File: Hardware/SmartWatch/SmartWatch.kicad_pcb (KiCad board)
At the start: 2 copper layers, 31 parts, among them IC1 DA14683-00000U22, IC2 SPG08P4HM4H-1, IC3 MC3630, J1 Charging Port, M1 c0720b001f, Q1 ECH8693R-TL-W, Q2 ECH8693R-TL-W, U1 BQ297xy, U2 ATmega328P-MMH, U3 W25Q128JVS, U4 MAX30100EFD+, Y1 16Mhz

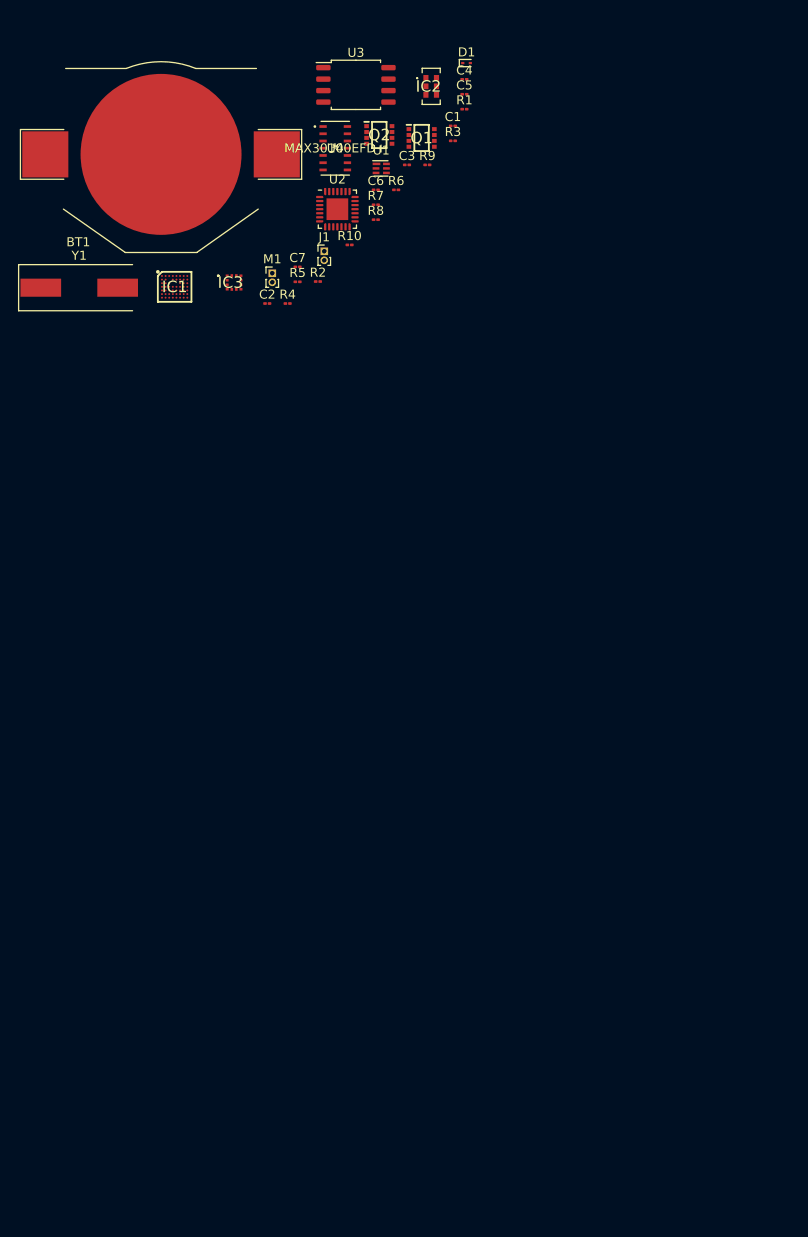
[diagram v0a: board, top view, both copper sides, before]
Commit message: [Update] Wired Display connector to MCU.
Communication type: SPI
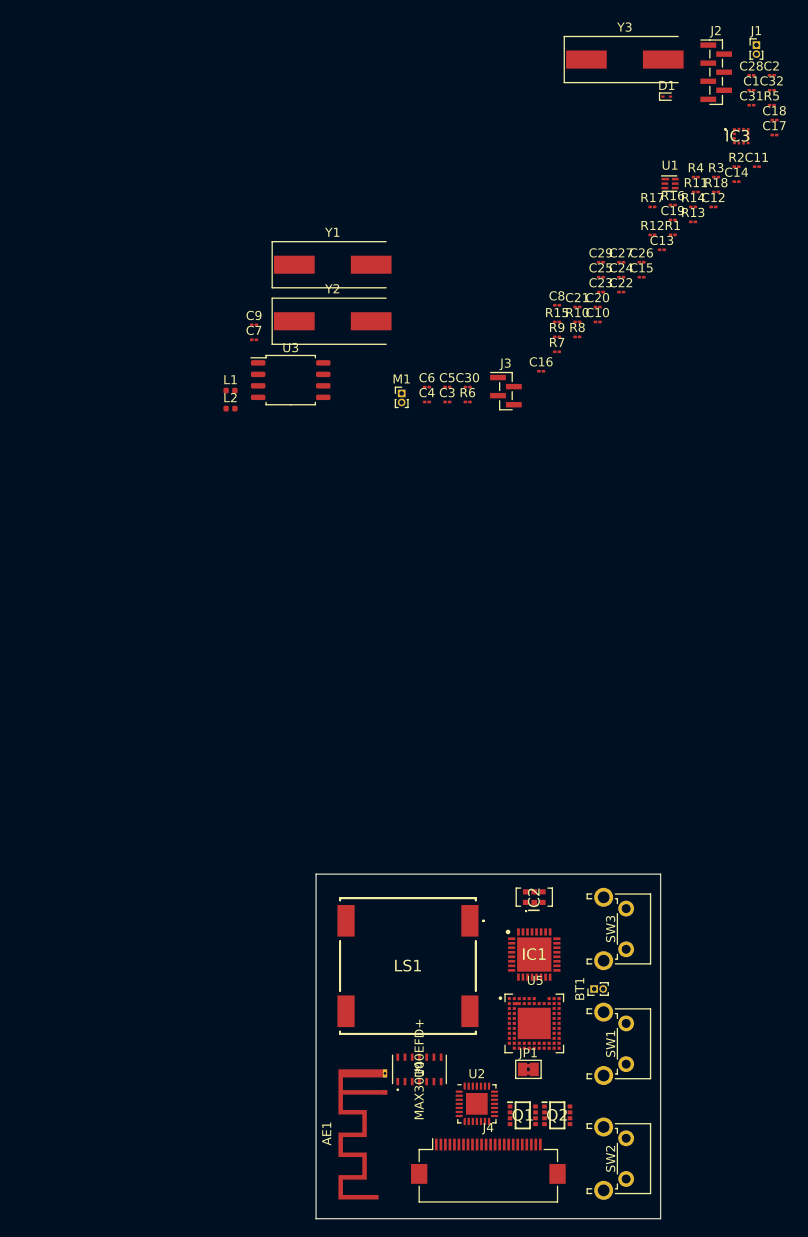
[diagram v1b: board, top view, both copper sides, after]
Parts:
- added AE1: Antenna, RF_Antenna:Texas_SWRA117D_2.4GHz_Left, F.Cu at (109.2, 74.9)
- added C10: 1uF, Capacitor_SMD:C_01005_0402Metric, F.Cu at (132.7, -10.3)
- added C11: 1uF, Capacitor_SMD:C_01005_0402Metric, F.Cu at (150.3, -27.4)
- added C12: 4.7uF, Capacitor_SMD:C_01005_0402Metric, F.Cu at (145.5, -23.0)
- added C13: 4.7uF, Capacitor_SMD:C_01005_0402Metric, F.Cu at (139.8, -18.2)
- added C14: 10uF, Capacitor_SMD:C_01005_0402Metric, F.Cu at (148.1, -25.8)
- added C15: 10uF, Capacitor_SMD:C_01005_0402Metric, F.Cu at (137.6, -15.2)
- added C16: 4.7uF, Capacitor_SMD:C_01005_0402Metric, F.Cu at (126.5, -4.81)
- added C17: 10uF, Capacitor_SMD:C_01005_0402Metric, F.Cu at (152.3, -30.9)
- added C18: 100nF, Capacitor_SMD:C_01005_0402Metric, F.Cu at (152.3, -32.6)
- added C19: 10nF, Capacitor_SMD:C_01005_0402Metric, F.Cu at (141.0, -21.5)
- added C20: 10nF, Capacitor_SMD:C_01005_0402Metric, F.Cu at (132.7, -11.9)
- added C21: C, Capacitor_SMD:C_01005_0402Metric, F.Cu at (130.5, -11.9)
- added C22: C, Capacitor_SMD:C_01005_0402Metric, F.Cu at (135.3, -13.6)
- added C23: 10uF, Capacitor_SMD:C_01005_0402Metric, F.Cu at (133.1, -13.6)
- added C24: 0.1uF, Capacitor_SMD:C_01005_0402Metric, F.Cu at (135.3, -15.2)
- added C25: 10uF, Capacitor_SMD:C_01005_0402Metric, F.Cu at (133.1, -15.2)
- added C26: 0.1uF, Capacitor_SMD:C_01005_0402Metric, F.Cu at (137.6, -16.9)
- added C27: 0.1uF, Capacitor_SMD:C_01005_0402Metric, F.Cu at (135.3, -16.9)
- added C28: 10uF, Capacitor_SMD:C_01005_0402Metric, F.Cu at (149.7, -37.5)
- added C29: 10uF, Capacitor_SMD:C_01005_0402Metric, F.Cu at (133.1, -16.9)
- added C30: 10uF, Capacitor_SMD:C_01005_0402Metric, F.Cu at (118.4, -3.06)
- added C31: 0.1uF, Capacitor_SMD:C_01005_0402Metric, F.Cu at (149.7, -34.2)
- added C32: 0.1uF, Capacitor_SMD:C_01005_0402Metric, F.Cu at (152.0, -35.9)
- added C8: 4.7uF, Capacitor_SMD:C_01005_0402Metric, F.Cu at (128.2, -12.1)
- added C9: 1uF, Capacitor_SMD:C_01005_0402Metric, F.Cu at (94.7, -9.94)
- added J2: DA_PROG_CONN, Connector_PinHeader_1.00mm:PinHeader_1x07_P1.00mm_Vertical_SMD_Pin1Left, F.Cu at (145.8, -37.9)
- added J3: ARD_PROG_CONN, Connector_PinHeader_1.00mm:PinHeader_1x04_P1.00mm_Vertical_SMD_Pin1Left, F.Cu at (122.6, -2.61)
- added J4: Adafruit 4520, Connector_FFC-FPC:Hirose_FH12-24S-0.5SH_1x24-1MP_P0.50mm_Horizontal, F.Cu at (120.7, 82.5)
- added JP1: Jumper, Jumper:SolderJumper-2_P1.3mm_Bridged2Bar_Pad1.0x1.5mm, F.Cu at (125.1, 72.4)
- added L1: 470nH, Inductor_SMD:L_0402_1005Metric, F.Cu at (92.1, -2.67)
- added L2: 470nH, Inductor_SMD:L_0402_1005Metric, F.Cu at (92.1, -0.68)
- added LS1: SMS-1508MS-HT-R, SamacSys_Parts:SMS1508MSHTR, F.Cu at (111.8, 61.0)
- added R11: 100m, Resistor_SMD:R_01005_0402Metric, F.Cu at (143.6, -24.6)
- added R12: 10K, Resistor_SMD:R_01005_0402Metric, F.Cu at (138.8, -19.9)
- added R13: 10K, Resistor_SMD:R_01005_0402Metric, F.Cu at (143.3, -21.3)
- added R14: 10K, Resistor_SMD:R_01005_0402Metric, F.Cu at (143.3, -23.0)
- added R15: 10K, Resistor_SMD:R_01005_0402Metric, F.Cu at (128.2, -10.3)
- added R16: 3.3K, Resistor_SMD:R_01005_0402Metric, F.Cu at (141.0, -23.2)
- added R17: 3.3K, Resistor_SMD:R_01005_0402Metric, F.Cu at (138.8, -23.0)
- added R18: 3.3K, Resistor_SMD:R_01005_0402Metric, F.Cu at (145.8, -24.6)
- added SW1: SW_MEC_5E, Button_Switch_THT:SW_Tactile_SPST_Angled_PTS645Vx58-2LFS, F.Cu at (135.9, 67.3)
- added SW2: SW_MEC_5E, Button_Switch_THT:SW_Tactile_SPST_Angled_PTS645Vx58-2LFS, F.Cu at (135.9, 80.0)
- added SW3: SW_MEC_5E, Button_Switch_THT:SW_Tactile_SPST_Angled_PTS645Vx58-2LFS, F.Cu at (135.9, 54.6)
- added U5: DA14683-00000A92, DA14683-00000A92:XCVR_DA14680-01F08A92, F.Cu at (125.7, 67.3)
- added Y2: 16Mhz, Crystal:Crystal_SMD_HC49-SD, F.Cu at (103.4, -10.3)
- added Y3: 32.768Mhz, Crystal:Crystal_SMD_HC49-SD, F.Cu at (135.7, -39.3)
- BT1: footprint Battery:BatteryHolder_Keystone_3002_1x2032 -> Connector_PinHeader_1.00mm:PinHeader_1x02_P1.00mm_Vertical
- C7: value C -> 100nF
- IC1: value DA14683-00000U22 -> 6PAIC3109TWRHMRQ1; footprint SamacSys_Parts:BGA53C40P8X7_341X301X55 -> SamacSys_Parts:QFN50P500X500X90-33N-D
- moved Q2 110.2 mm to (128.3, 77.5)
- moved Q1 108.7 mm to (124.5, 77.5)
- moved BT1 104.0 mm to (132.3, 63.5), turned to 90 degrees
- moved U4 102.3 mm to (113.0, 72.4), turned to 90 degrees
- moved U2 100.1 mm to (119.4, 76.2)
- moved IC2 90.4 mm to (125.7, 53.3), turned to 90 degrees
- moved IC1 83.9 mm to (125.7, 59.7)
- moved C2 61.2 mm to (152.0, -37.5)
- moved IC3 58.4 mm to (148.6, -30.8)
- moved R5 56.0 mm to (152.0, -34.2)
- moved J1 53.0 mm to (150.3, -40.9)
- moved R2 48.0 mm to (148.1, -27.4)
- moved R4 47.3 mm to (143.6, -26.3)
- moved C4 35.9 mm to (113.9, -1.41)
- moved U3 33.4 mm to (98.8, -3.83)
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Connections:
- net /MOTOR_DRIVE renamed /P1_0
- C2 pad 2: GNDREF -> GND
- C3 pad 2: GNDREF -> GND
- C4 pad 1: GNDREF -> GND
- C5 pad 1: GNDREF -> GND
- C6 pad 2: GNDREF -> GND
- C7 pad 2: GNDREF -> GND
- D1 pad 2: GNDREF -> GND
- IC2 pad 2: GNDREF -> GND
- IC2 pad 3: /MIC_DATA -> /P4_2
- IC2 pad 4: /MIC_CLK -> /P4_1
- IC2 pad 5: GNDREF -> GND
- IC2 pad 6: /MIC_SELECT -> /P4_0
- IC3 pad 1: GNDREF -> GND
- IC3 pad 12: /ACCEL_SCL -> /P3_7
- IC3 pad 2: /ACCEL_SDA -> /P3_5
- IC3 pad 9: GNDREF -> GND
- J1 pad 1: GNDREF -> GND
- Q2 pad 1: GNDREF -> GND
- Q2 pad 3: GNDREF -> GND
- R10 pad 1: /ACCEL_SDA -> /P3_5
- R6 pad 1: GNDREF -> GND
- R9 pad 1: /ACCEL_SCL -> /P3_7
- U2 pad 1: Net-(U2-Pad1) -> /SPEAKER
- U2 pad 16: Net-(U2-Pad16) -> +3V3
- U2 pad 17: Net-(U2-Pad17) -> +3V3
- U2 pad 23: Net-(U2-Pad23) -> /P3_5
- U2 pad 24: Net-(U2-Pad24) -> /P3_7
- U2 pad 25: Net-(U2-Pad25) -> /ARD_RST
- U2 pad 26: Net-(U2-Pad26) -> /ARD_RX
- U2 pad 27: Net-(U2-Pad27) -> /ARD_TX
- U3 pad 2: /QSPI_IO1 -> /P0_2
- U3 pad 3: /QSPI_IO2 -> /P0_3
- U3 pad 4: GNDREF -> GND
- U3 pad 5: /QSPI_IO0 -> /P0_1
- U3 pad 6: /QSPI_CLK -> /P0_0
- U3 pad 7: /QSPI_IO3 -> /P0_4
- U4 pad 12: GNDREF -> GND
- U4 pad 13: /HEART_INT -> /P4_3
- U4 pad 2: /HEART_SCL -> /P3_7
- U4 pad 3: /HEART_SDA -> /P3_5
- U4 pad 4: GNDA -> GND
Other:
- board outline added: 38.1 x 38.1 mm
